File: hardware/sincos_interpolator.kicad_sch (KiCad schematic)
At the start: 53 parts, among them J1 SIN, J10 RJ45_Shielded, J2 COS, J3 ZERO, J4 POWER IN, J5 POWER OUT, J6 A, J7 B, J8 Z, J9 RJ45_Shielded, Q1 TIC116, U1 iC-NV, U2 MC3487DX

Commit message: New component references and fab outputs
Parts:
- JP11: renamed from JP6; value SIN_VREF -> SIN VREF
- JP21: renamed from JP7; value COS_VREF -> COS VREF
- renumbered D4 to D11, D5 to D21, D6 to D31, J4 to J1, J1 to J11, J6 to J12, J5 to J2, J2 to J21, J7 to J22, J10 to J3, J3 to J31, J8 to J32, J9 to J4, JP9 to JP12, JP12 to JP13, JP10 to JP22, JP13 to JP23, JP11 to JP32, JP14 to JP33, JP8 to JP6, R5 to R1, R1 to R11, R2 to R12, R8 to R13, R6 to R2, R3 to R21, R4 to R22, R9 to R23, R7 to R3, R10 to R33

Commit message: Corrected MC3487DX power polarity and separated shield
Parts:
- added JP7, JP9: SHIELD GND, Jumper:SolderJumper-2_P1.3mm_Open_RoundedPad1.0x1.5mm, symbol Jumper:SolderJumper_2_Open
- added JP8: SHIELD CONNECT, Jumper:SolderJumper-2_P1.3mm_Open_RoundedPad1.0x1.5mm, symbol Jumper:SolderJumper_2_Open
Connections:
- net +5V: now also C5.2, U2.16 (VCC), U2.16 (VCC), U2.16 (VCC), U2.16 (VCC); no longer C5.1, U2.8 (GND), U2.8 (GND), U2.8 (GND), U2.8 (GND)
- net GND: now also C5.1, U2.8 (GND), U2.8 (GND), U2.8 (GND), U2.8 (GND), JP7.2 (B), JP9.2 (B); no longer C5.2, J1.1 (Pin_1), J2.3 (Pin_3), J3.SH, J4.SH, U2.16 (VCC), U2.16 (VCC), U2.16 (VCC), U2.16 (VCC)
- new net SHIELD_IN: J1.1 (Pin_1), J4.SH, JP7.1 (A), JP8.1 (A)
- new net SHIELD_OUT: J2.3 (Pin_3), J3.SH, JP8.2 (B), JP9.1 (A)
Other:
- note added: "(note: MC3487DX symbol is strangely drawn with regards to power/gnd)"
- moved on the sheet: C1, C2, C3, C4, C5, D1, D11, D2, D21, D3, D31, F1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

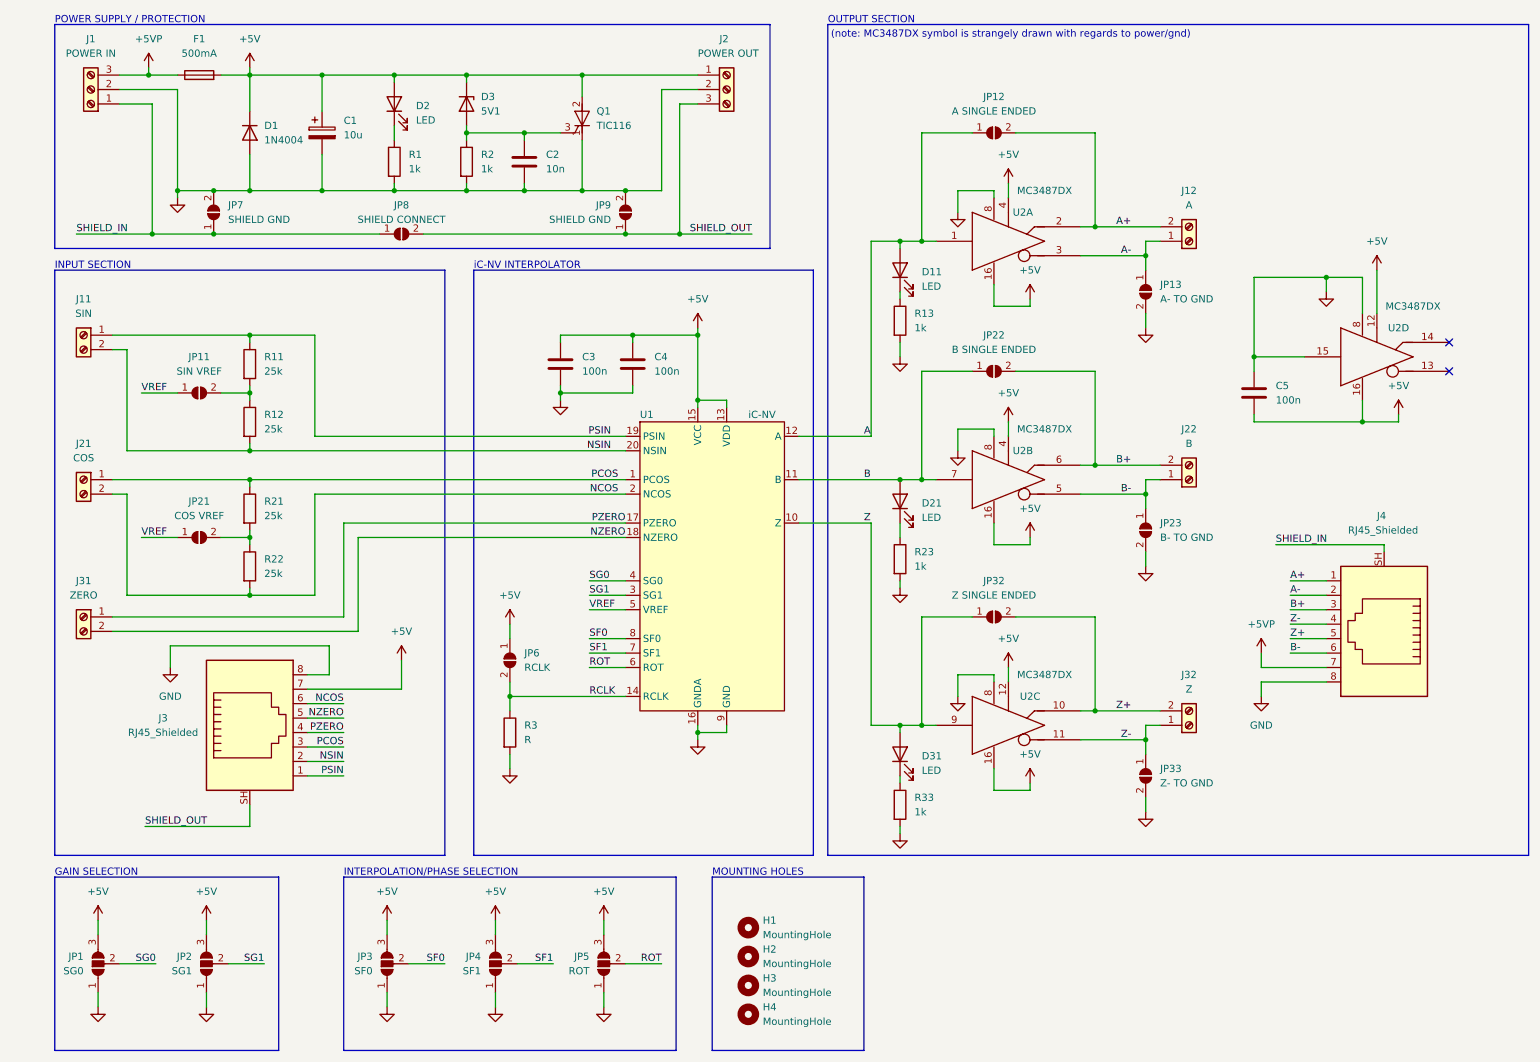
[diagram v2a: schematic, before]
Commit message: RJ45 jacks rotated 180 degrees
RJ45 jacks rotated 180 degrees to allow the used of angled RJ45 jacks
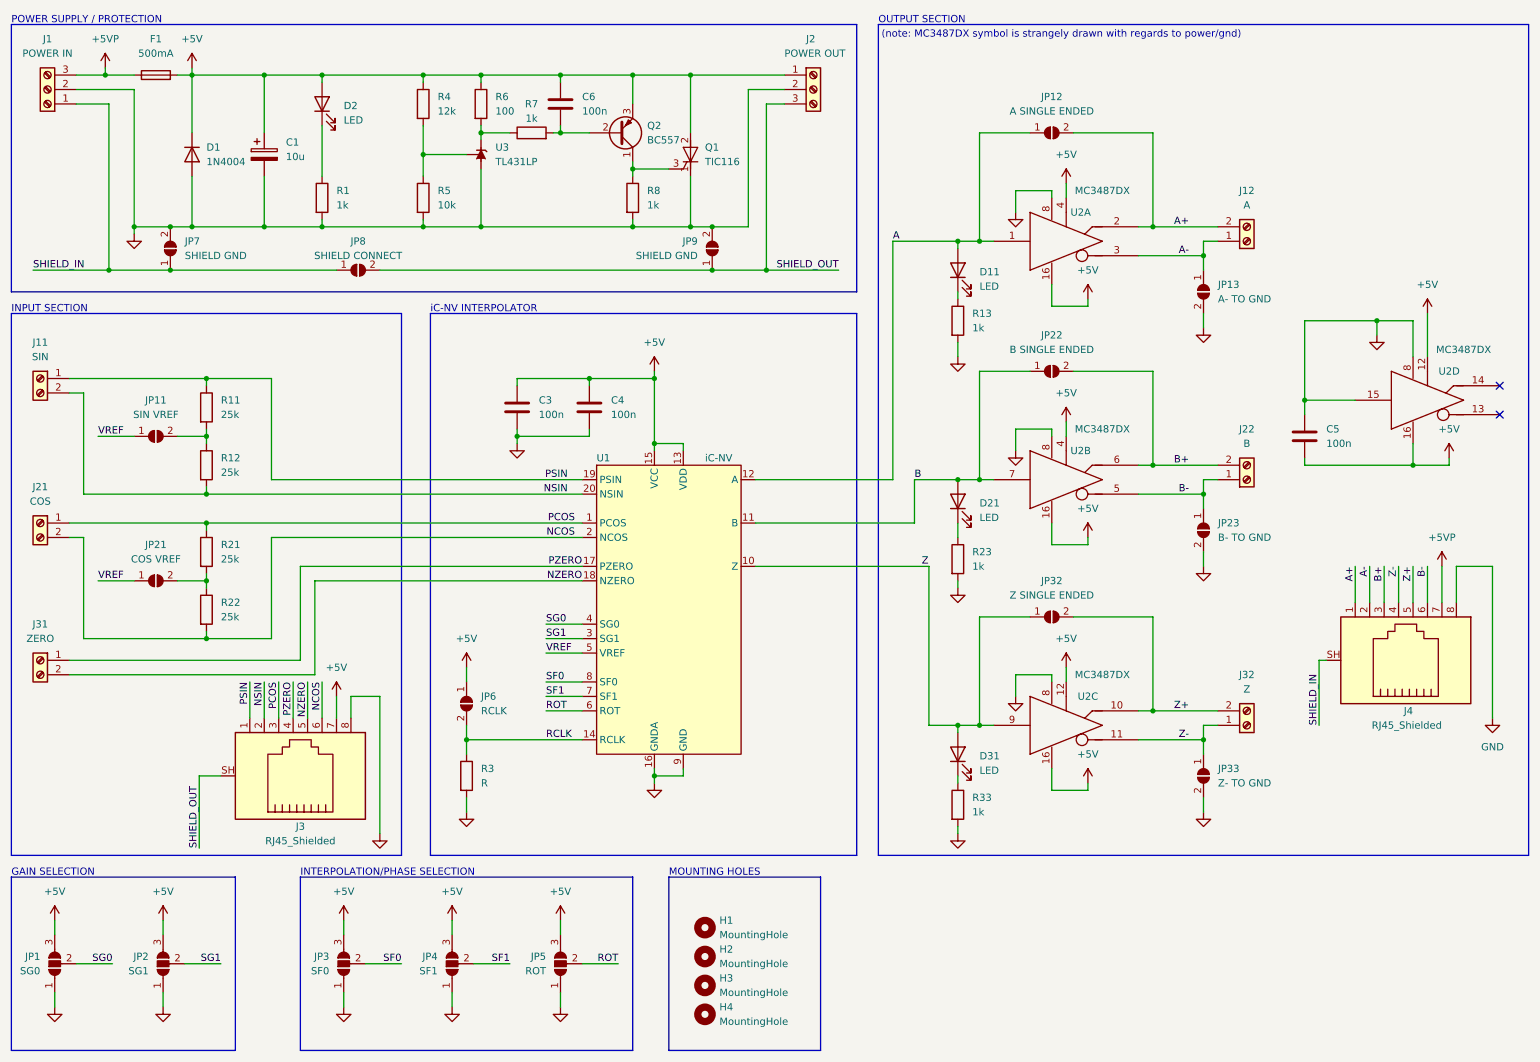
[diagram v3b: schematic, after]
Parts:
- removed C2: 10n, Capacitor_THT:C_Disc_D5.0mm_W2.5mm_P2.50mm, symbol Device:C
- removed D3: 5V1, Diode_THT:D_DO-35_SOD27_P7.62mm_Horizontal, symbol Device:D_Zener
- removed R2: 1k, Resistor_THT:R_Axial_DIN0207_L6.3mm_D2.5mm_P10.16mm_Horizontal, symbol Device:R
- added C6: 100n, Capacitor_THT:C_Disc_D5.0mm_W2.5mm_P2.50mm, symbol Device:C
- added Q2: BC557, Package_TO_SOT_THT:TO-92_Inline, symbol Transistor_BJT:BC557
- added R4: 12k, Resistor_THT:R_Axial_DIN0207_L6.3mm_D2.5mm_P10.16mm_Horizontal, symbol Device:R
- added R5: 10k, Resistor_THT:R_Axial_DIN0207_L6.3mm_D2.5mm_P10.16mm_Horizontal, symbol Device:R
- added R6: 100, Resistor_THT:R_Axial_DIN0207_L6.3mm_D2.5mm_P10.16mm_Horizontal, symbol Device:R
- added R7, R8: 1k, Resistor_THT:R_Axial_DIN0207_L6.3mm_D2.5mm_P10.16mm_Horizontal, symbol Device:R
- added U3: TL431LP, Package_TO_SOT_THT:TO-92_Inline, symbol Reference_Voltage:TL431LP
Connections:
- net +5V: now also C6.1, Q2.3 (E), R4.1, R6.1
- net GND: now also R5.2, R8.2, U3.2 (A)
- net at Q1.3 (G): now also Q2.1 (C), R8.1
- new net: C6.2, Q2.2 (B), R7.2
- new net: R6.2, R7.1, U3.3 (K)
- new net: R4.2, R5.1, U3.1 (REF)
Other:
- moved on the sheet: C1, C3, C4, C5, D1, D11, D2, D21, D31, F1, H1, H2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
